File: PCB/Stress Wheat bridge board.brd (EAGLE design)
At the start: 69.5 x 69.8 mm, 12 parts, among them IC2 ICL7663CPA

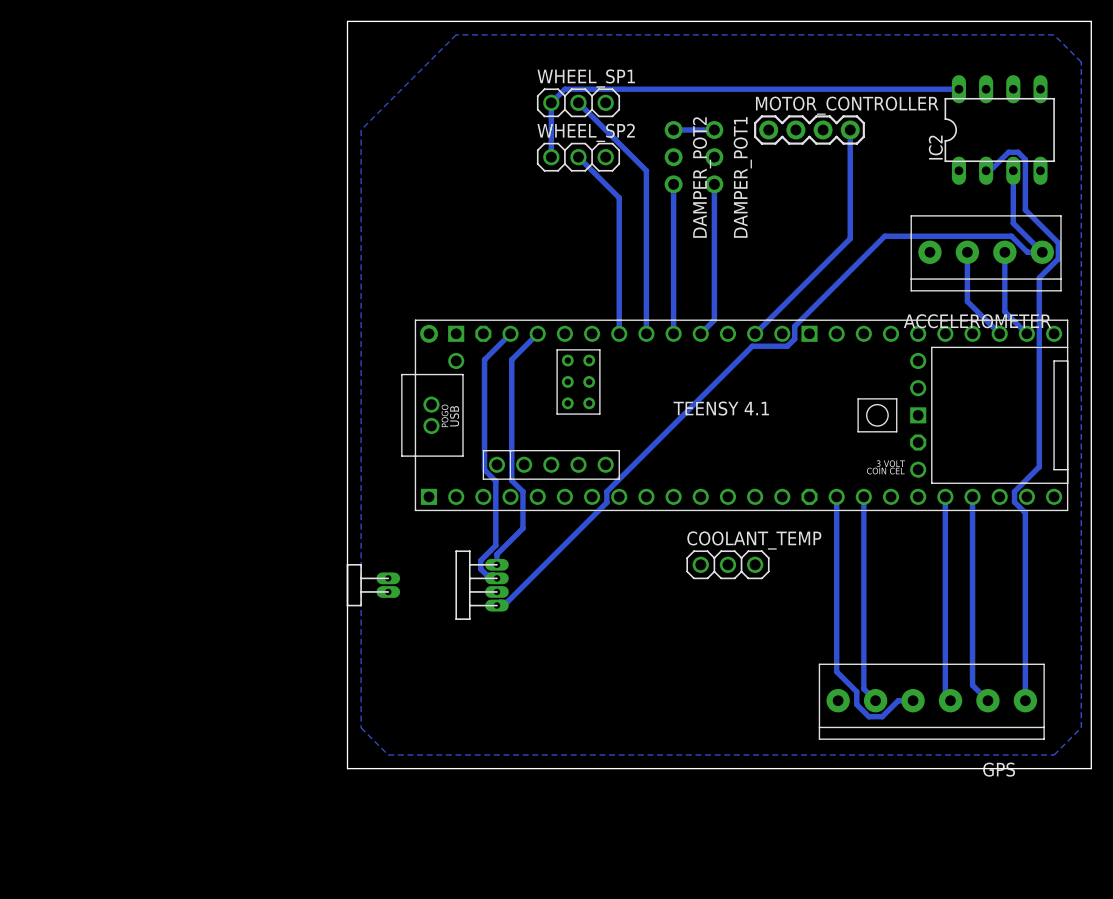
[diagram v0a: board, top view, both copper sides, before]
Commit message: Stress board for Wheat bridge and edits
Created the Wheat bridge board with the different stress gauges in the F-E library. There were some minor edits that the other boards needed as well.
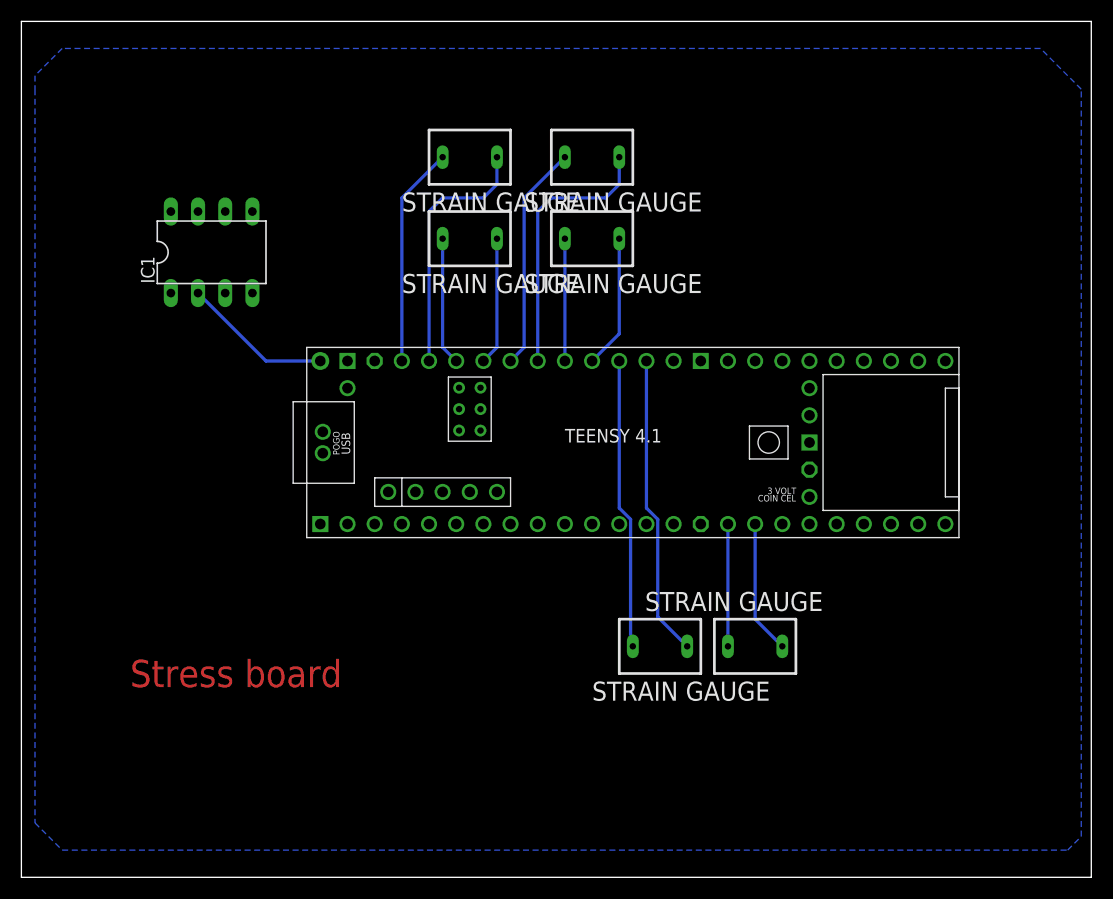
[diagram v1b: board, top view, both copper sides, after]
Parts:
- removed ACCELEROMETER: 1X4-3.5MM, adafruit:1X04-3.5MM
- removed CAN1_CLCH: CAN_BUS, F-E library custom components:CAN_BUS
- removed CAN1_TEE: CAN_TEE, F-E library custom components:CAN_TEN
- removed COOLANT_TEMP, WHEEL_SP1, WHEEL_SP2: (no value), adafruit:1X03
- removed DAMPER_POT1, DAMPER_POT2: (no value), adafruit:1X03-CLEANBIG
- removed GPS: (no value), adafruit:1X06-3.5MM
- removed IC2: ICL7663CPA, maxim:DIL08
- removed MOTOR_CONTROLLER: 1X4-BIG, adafruit:1X04-BIG
- added IC1: ICL7663CPA, maxim:DIL08
- added U$2, U$4, U$5, U$6, U$7: STR_GAUGE, F-E library custom components:STR_GAUGE
- added U$3: TEENSY41, teensy:TEENSY41
- U$1: value TEENSY41 -> STR_GAUGE; device teensy:TEENSY41 -> F-E library custom components:STR_GAUGE
- moved U$1 23.3 mm to (59.7, 21.6)
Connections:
- removed net 3.3V: ACCELEROMETER.4, CAN1_TEE.P$1, IC2.3
- removed net A2: DAMPER_POT1.3, U$1.16-A2/RX4/SCL1
- removed net A3: DAMPER_POT2.3, U$1.17-A3/TX4/SDA1
- removed net A_MC: MOTOR_CONTROLLER.4, U$1.14-A0/TX3/SPDIF_OUT
- removed net BR_VCC: DAMPER_POT1.1, DAMPER_POT2.1
- removed net N$2: CAN1_TEE.P$3, U$1.23-A9/CRX1/MCLK1
- removed net N$3: CAN1_TEE.P$4, U$1.22-A8/CTX1
- removed net RX: ACCELEROMETER.2, U$1.35-TX8
- removed net RX_2: GPS.5, U$1.29-TX7
- removed net SCL: GPS.3, U$1.24-A10/TX6/SCL2
- removed net SDA: GPS.2, U$1.25-A11/RX6/SDA2
- removed net TX: ACCELEROMETER.3, U$1.34-RX8
- removed net TX_2: GPS.4, U$1.28-RX7
- removed net WH_SP1_D: U$1.18-A4/SDA0, WHEEL_SP1.2
- removed net WH_SP2_D: U$1.19-A5/SCL0, WHEEL_SP2.2
- new net STR1_H: U$1.P$1, U$3.15-A1/RX3/SPDIF_IN
- new net STR1_L: U$1.P$2, U$3.14-A0/TX3/SPDIF_OUT
- new net STR2_H: U$2.P$1, U$3.17-A3/TX4/SDA1
- new net STR2_L: U$2.P$2, U$3.16-A2/RX4/SCL1
- new net STR3_H: U$3.19-A5/SCL0, U$4.P$1
- new net STR3_L: U$3.18-A4/SDA0, U$4.P$2
- new net STR4_H: U$3.21-A7/RX5/BCLK1, U$5.P$1
- new net STR4_L: U$3.20-A6/TX5/LRCLK1, U$5.P$2
- new net STR5_H: U$3.23-A9/CRX1/MCLK1, U$6.P$1
- new net STR5_L: U$3.22-A8/CTX1, U$6.P$2
- new net STR6_H: U$3.25-A11/RX6/SDA2, U$7.P$1
- new net STR6_L: U$3.24-A10/TX6/SCL2, U$7.P$2
- net 12V: now also IC1.8; no longer IC2.8, WHEEL_SP1.1, WHEEL_SP2.1
- net 5V: now also IC1.2, U$3.VIN; no longer GPS.6, IC2.2
- net GND: now also IC1.4, U$3.GND1, U$3.GND2, U$3.GND3, U$3.GND4, U$3.GND5, U$3.GND6; no longer ACCELEROMETER.1, CAN1_TEE.P$2, COOLANT_TEMP.3, DAMPER_POT1.2, DAMPER_POT2.2, GPS.1, IC2.4, MOTOR_CONTROLLER.1, U$1.GND1, U$1.GND2, U$1.GND3, U$1.GND4, U$1.GND5, U$1.GND6, WHEEL_SP1.3, WHEEL_SP2.3
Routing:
- net 3.3V: track 75.9 -> 0.00 mm
- net 5V: track 58.6 -> 14.1 mm
- net 12V: track 43.7 -> 0.00 mm
- net STR1_L: track 0.00 -> 28.2 mm
- net STR1_H: track 0.00 -> 27.2 mm
- net SCL: track 26.5 -> 0.00 mm
- net N$2: track 25.9 -> 0.00 mm
- net STR3_L: track 0.00 -> 25.2 mm
- net WH_SP1_D: track 24.2 -> 0.00 mm
- net N$3: track 24.0 -> 0.00 mm
- net STR5_L: track 0.00 -> 23.9 mm
- net A_MC: track 22.7 -> 0.00 mm
- net STR3_H: track 0.00 -> 21.2 mm
- net STR5_H: track 0.00 -> 20.6 mm
- net RX_2: track 19.6 -> 0.00 mm
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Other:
- board size 69.5 x 69.8 mm -> 100 x 80 mm
- board text added: "Stress board"
